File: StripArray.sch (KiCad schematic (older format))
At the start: 21 parts, among them U1 WS2811

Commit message: Invert Output using extra fet stage
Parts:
- removed JP?: Set_Low_Speed_400kHz, symbol Jumper:SolderJumper_2_Open
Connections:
- wire segments 34 -> 31
- no-connect marks 0 -> 1
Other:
- moved on the sheet: C?, Q?, R?, U1

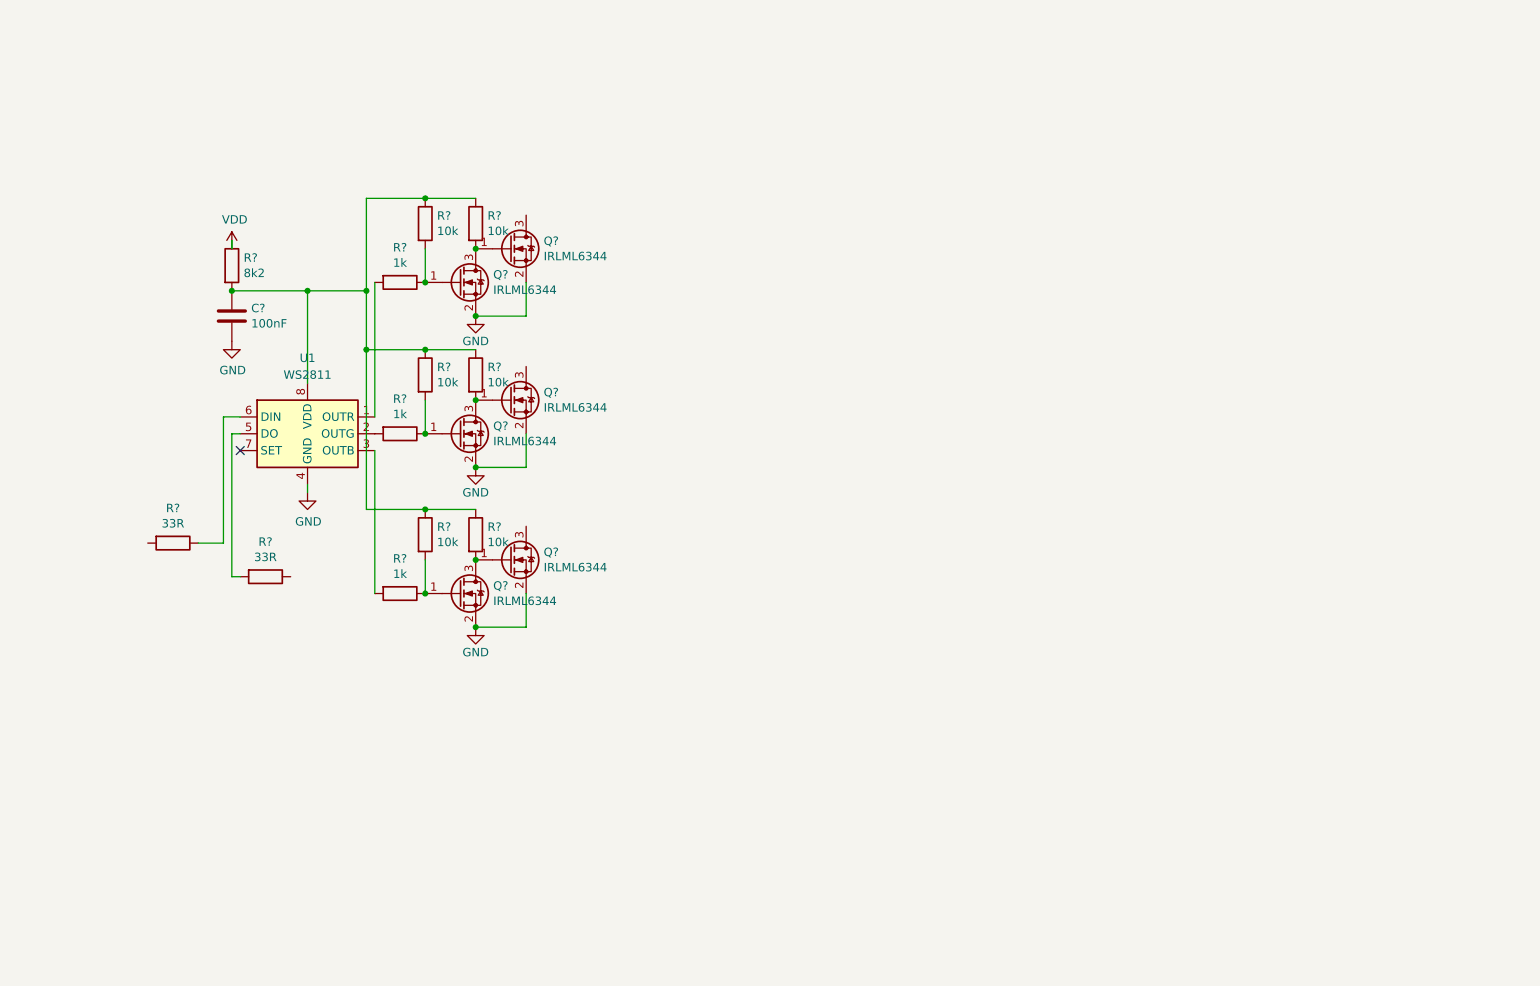
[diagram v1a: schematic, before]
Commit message: Added headers
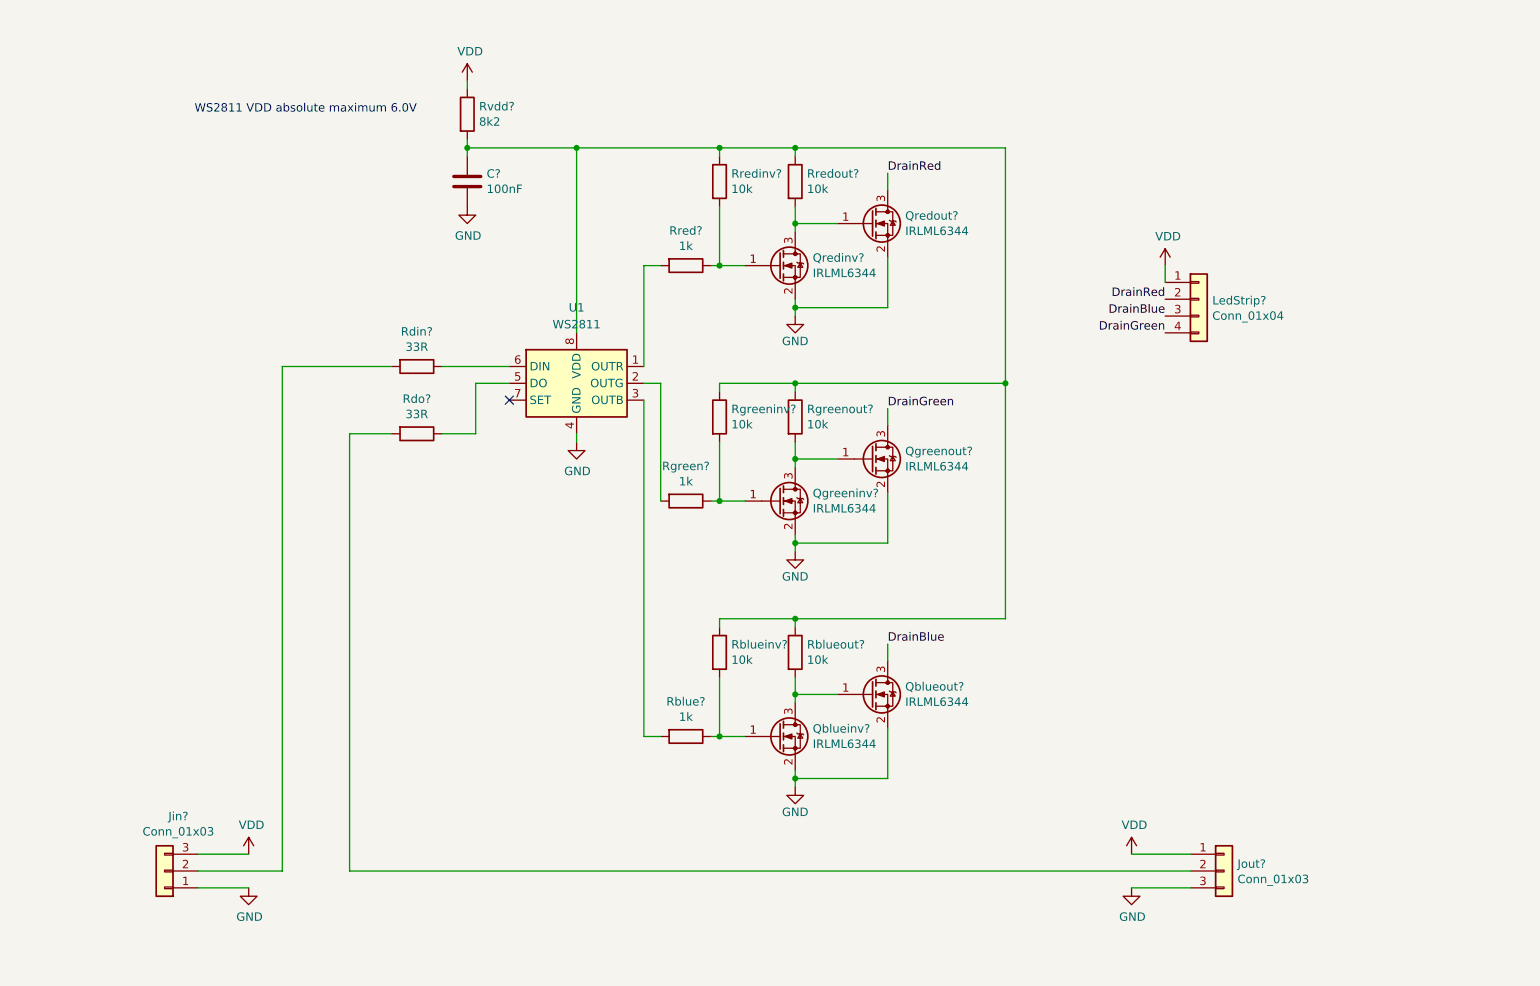
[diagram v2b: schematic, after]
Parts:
- removed Q? (x4): IRLML6344, Package_TO_SOT_SMD:SOT-23, symbol IRLML6344:IRLML6344
- removed R? (x4): 10k, Capacitors_SMD:C_0603_HandSoldering, symbol Device:R
- removed R? (x2): 1k, Capacitors_SMD:C_0603_HandSoldering, symbol Device:R
- added Jin?, Jout?: Conn_01x03, Pin_Headers:Pin_Header_Straight_1x03_Pitch2.54mm, symbol Connector_Generic:Conn_01x03
- added LedStrip?: Conn_01x04, StripArray:RGB_Strip, symbol Connector_Generic:Conn_01x04
- added Qblueinv?, Qblueout?, Qgreeninv?, Qgreenout?: IRLML6344, Package_TO_SOT_SMD:SOT-23, symbol IRLML6344:IRLML6344
- added Rblue?, Rgreen?: 1k, Capacitors_SMD:C_0603_HandSoldering, symbol Device:R
- added Rblueinv?, Rblueout?, Rgreeninv?, Rgreenout?: 10k, Capacitors_SMD:C_0603_HandSoldering, symbol Device:R
- gave numbers to parts that had none: 8
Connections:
- net GND: now also Jin?.1 (Pin_1), Jout?.3 (Pin_3), Qblueinv?.2 (S), Qblueout?.2 (S), Qgreeninv?.2 (S), Qgreenout?.2 (S)
- net VDD: now also Jin?.3 (Pin_3), Jout?.1 (Pin_1), LedStrip?.1 (Pin_1)
- net at U1.2 (OUTG): now also Rgreen?.2
- net at U1.3 (OUTB): now also Rblue?.2
- net at U1.5 (DO): now also Rdo?.1; no longer Rdo?.2
- net at C?.1, Rredinv?.1, Rredout?.1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: now also Rblueinv?.1, Rblueout?.1, Rgreeninv?.1, Rgreenout?.1
- net at Rdin?.2: now also Jin?.2 (Pin_2)
- net DrainRed: now reaches Qredout?.3 (D)
- net DrainRed: now also LedStrip?.2 (Pin_2)
- new net: Jout?.2 (Pin_2), Rdo?.2
- new net: Qgreeninv?.3 (D), Qgreenout?.1 (G), Rgreenout?.2
- new net: Qgreeninv?.1 (G), Rgreen?.1, Rgreeninv?.2
- new net: Qblueinv?.3 (D), Qblueout?.1 (G), Rblueout?.2
- new net: Qblueinv?.1 (G), Rblue?.1, Rblueinv?.2
- new net DrainBlue: LedStrip?.3 (Pin_3), Qblueout?.3 (D)
- new net DrainGreen: LedStrip?.4 (Pin_4), Qgreenout?.3 (D)
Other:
- note added: "WS2811 VDD absolute maximum 6.0V"
- moved on the sheet: C?, Qredinv?, Qredout?, Rdin?, Rdo?, Rred?, Rredinv?, Rredout?, Rvdd?, U1

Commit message: Led Driver addressable segment
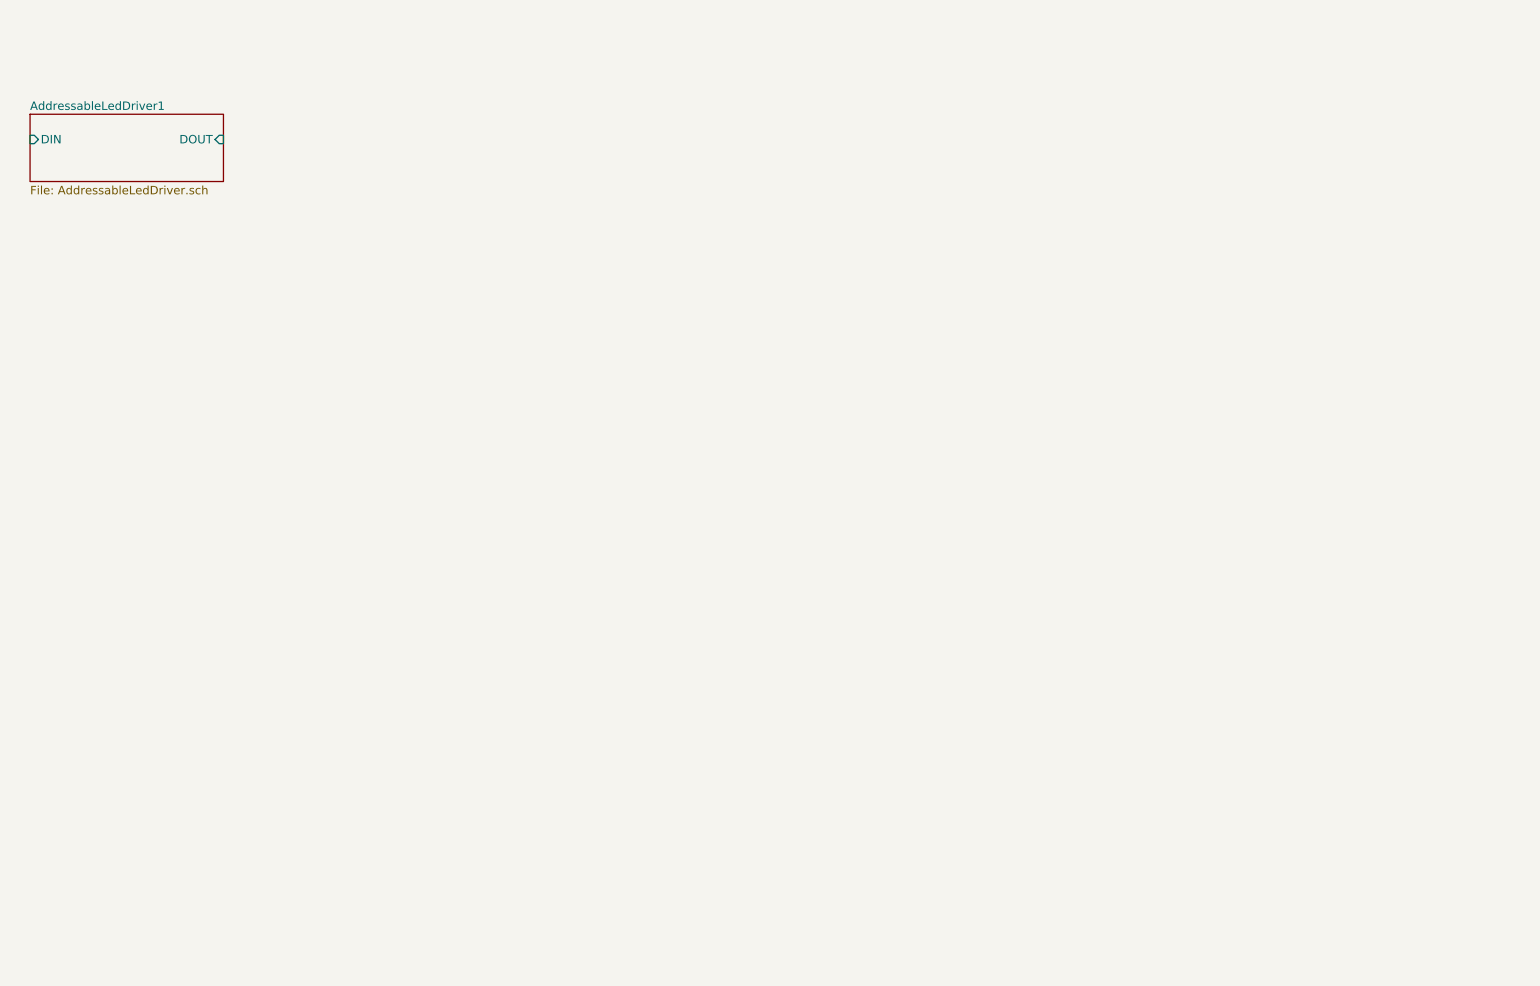
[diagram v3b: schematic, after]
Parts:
- removed C?: 100nF, Capacitors_SMD:C_0603_HandSoldering, symbol Device:C
- removed Jin?, Jout?: Conn_01x03, Pin_Headers:Pin_Header_Straight_1x03_Pitch2.54mm, symbol Connector_Generic:Conn_01x03
- removed LedStrip?: Conn_01x04, StripArray:RGB_Strip, symbol Connector_Generic:Conn_01x04
- removed Qblueinv?, Qblueout?, Qgreeninv?, Qgreenout?, Qredinv?, Qredout?: IRLML6344, Package_TO_SOT_SMD:SOT-23, symbol IRLML6344:IRLML6344
- removed Rblue?, Rgreen?, Rred?: 1k, Capacitors_SMD:C_0603_HandSoldering, symbol Device:R
- removed Rblueinv?, Rblueout?, Rgreeninv?, Rgreenout?, Rredinv?, Rredout?: 10k, Capacitors_SMD:C_0603_HandSoldering, symbol Device:R
- removed Rdin?, Rdo?: 33R, Capacitors_SMD:C_0603_HandSoldering, symbol Device:R
- removed Rvdd?: 8k2, Capacitors_SMD:C_0603_HandSoldering, symbol Device:R
- removed U1: WS2811, Housings_SOIC:SOIC-8_3.9x4.9mm_Pitch1.27mm, symbol Driver_LED:WS2811
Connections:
- no-connect marks 1 -> 0
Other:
- note removed: "WS2811 VDD absolute maximum 6.0V"

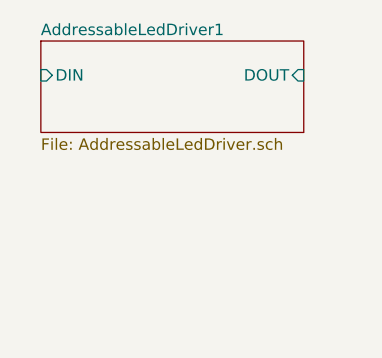
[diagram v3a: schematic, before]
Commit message: Restructure schema
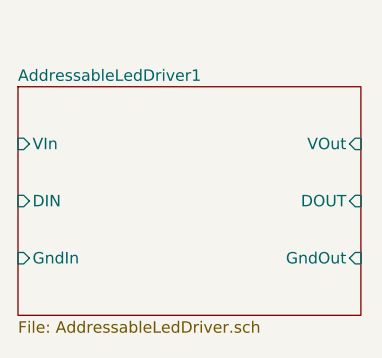
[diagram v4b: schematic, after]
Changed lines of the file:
@@
 $EndDescr
 $Sheet
-S 1100 1300 1150 400
+S 1000 1500 1500 1000
 U 60059F31
 F0 "AddressableLedDriver1" 50
 F1 "AddressableLedDriver.sch" 50
-F2 "DIN" I L 1100 1450 50
-F3 "DOUT" I R 2250 1450 50
+F2 "DIN" I L 1000 2000 50
+F3 "DOUT" I R 2500 2000 50
+F4 "VIn" I L 1000 1750 50
+F5 "VOut" I R 2500 1750 50
+F6 "GndIn" I L 1000 2250 50
+F7 "GndOut" I R 2500 2250 50
 $EndSheet
 $EndSCHEMATC

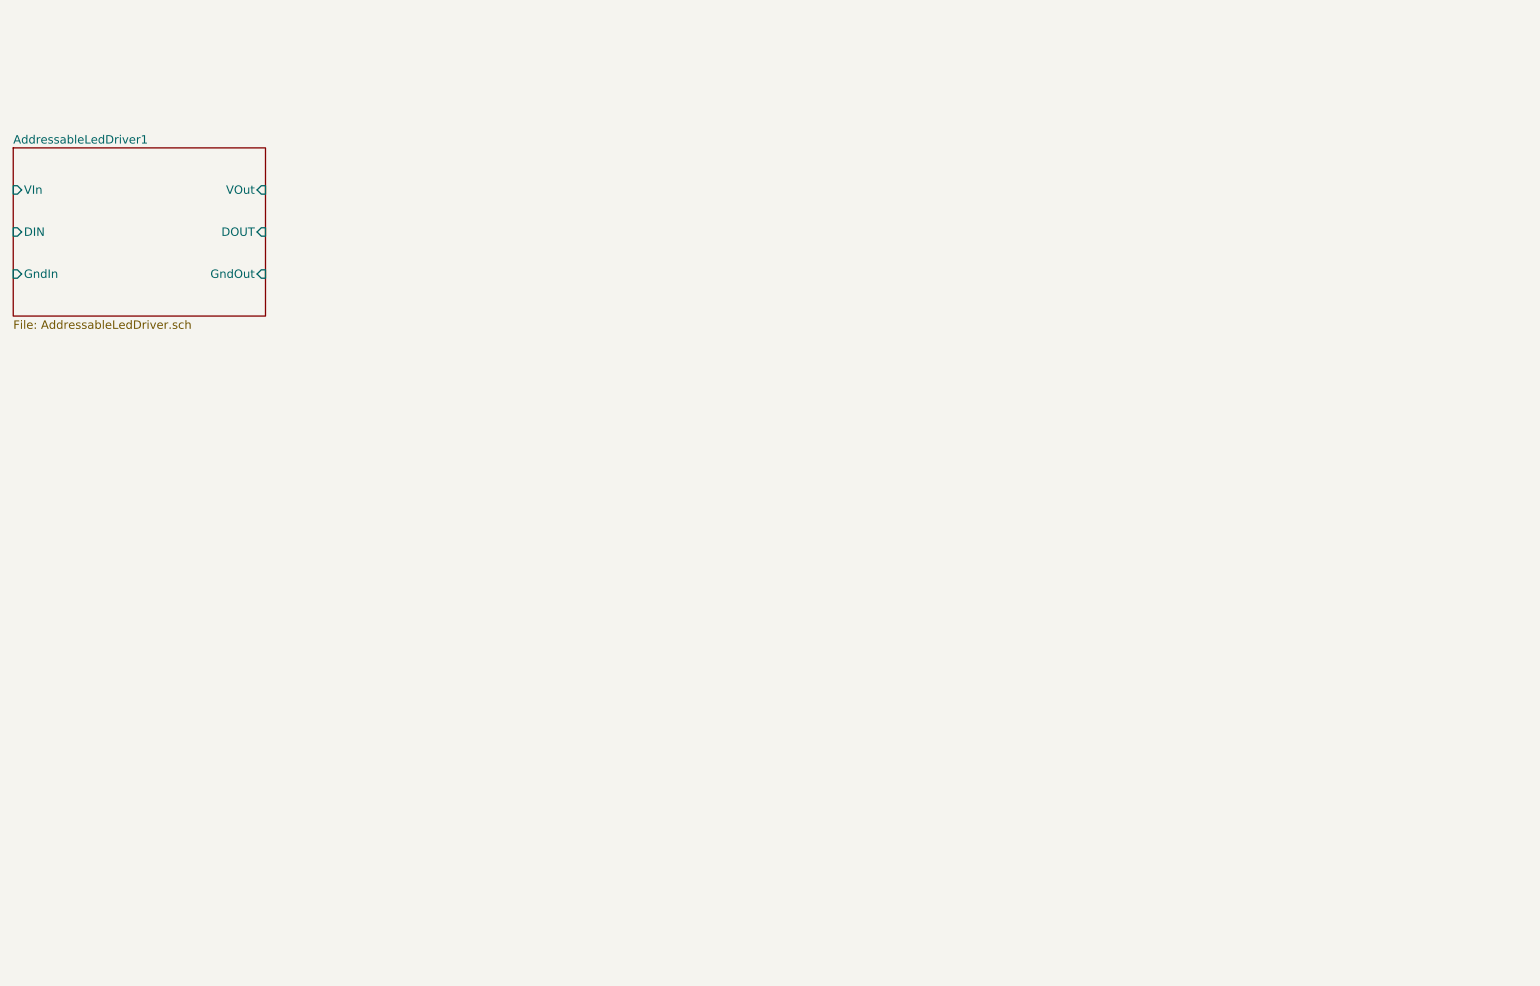
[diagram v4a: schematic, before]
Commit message: Add array of LED Driver
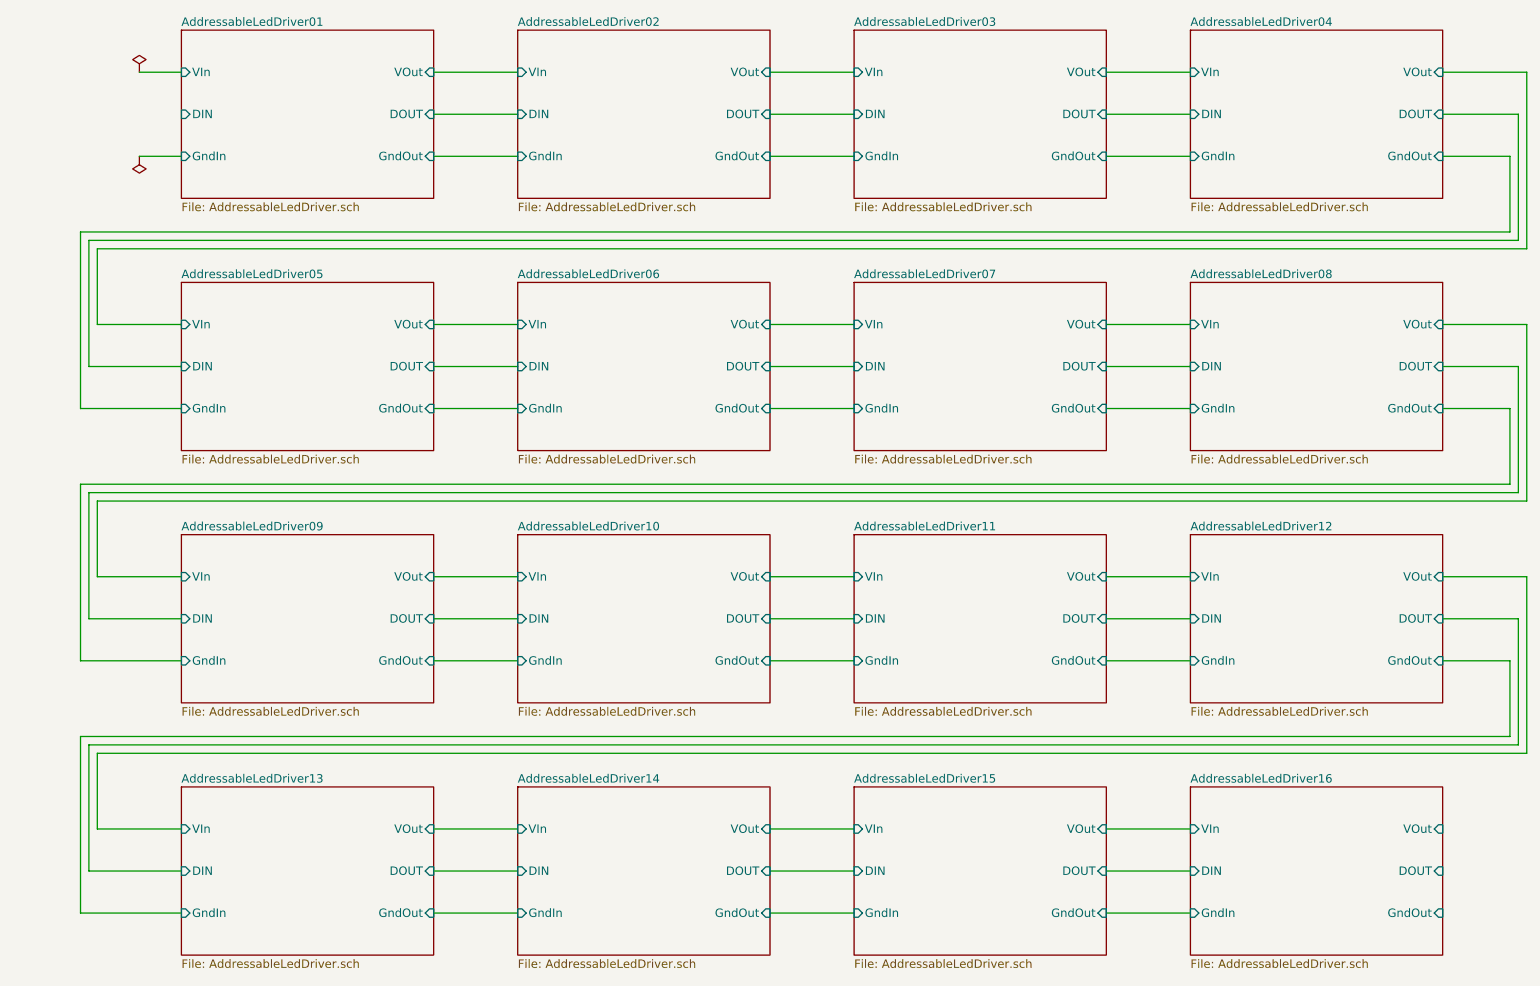
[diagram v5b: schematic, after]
